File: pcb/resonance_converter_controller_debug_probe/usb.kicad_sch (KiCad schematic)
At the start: 45 parts, among them J1 USB_C_Receptacle_USB2.0_14P, J3 USB_A, J4 USB_C_Receptacle_USB2.0_14P, J5 USB_C_Receptacle_PowerOnly_6P, Q1 Q_PMOS_GDS, Q2 Q_NMOS_GDS, Q3 Q_NMOS_GDS, U17 STUSB4500QTR, U18 USB6B1, U19 FT230XQ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

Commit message: Add schematic for debug probe
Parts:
- J3: footprint (none) -> Connector_USB:USB_A_Molex_67643_Horizontal
- U21, U22: footprint (none) -> Package_SO:TSSOP-8_4.4x3mm_P0.65mm
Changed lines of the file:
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@@
 			)
 		)
-		(property "Footprint" ""
+		(property "Footprint" "Package_SO:TSSOP-8_4.4x3mm_P0.65mm"
 			(at 176.53 121.92 0)
 			(effects
@@
 			)
 		)
-		(property "Footprint" ""
+		(property "Footprint" "Package_SO:TSSOP-8_4.4x3mm_P0.65mm"
 			(at 210.82 175.26 0)
 			(effects
@@
 			)
 		)
-		(property "Footprint" ""
+		(property "Footprint" "Connector_USB:USB_A_Molex_67643_Horizontal"
 			(at 243.84 135.89 0)
 			(effects

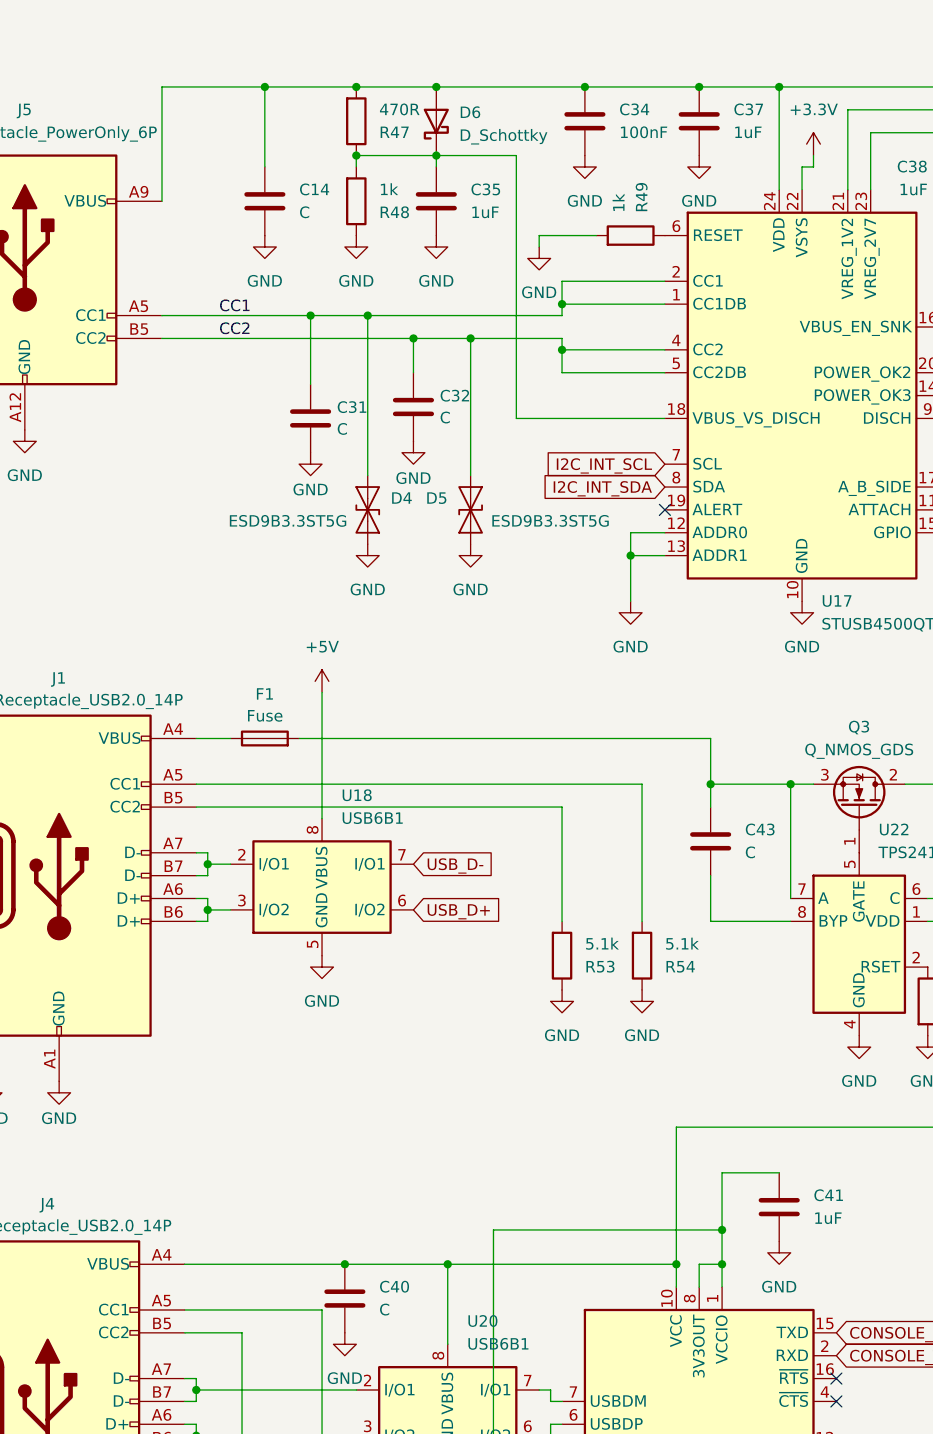
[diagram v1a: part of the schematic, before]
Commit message: Fix schematic and initial component layout
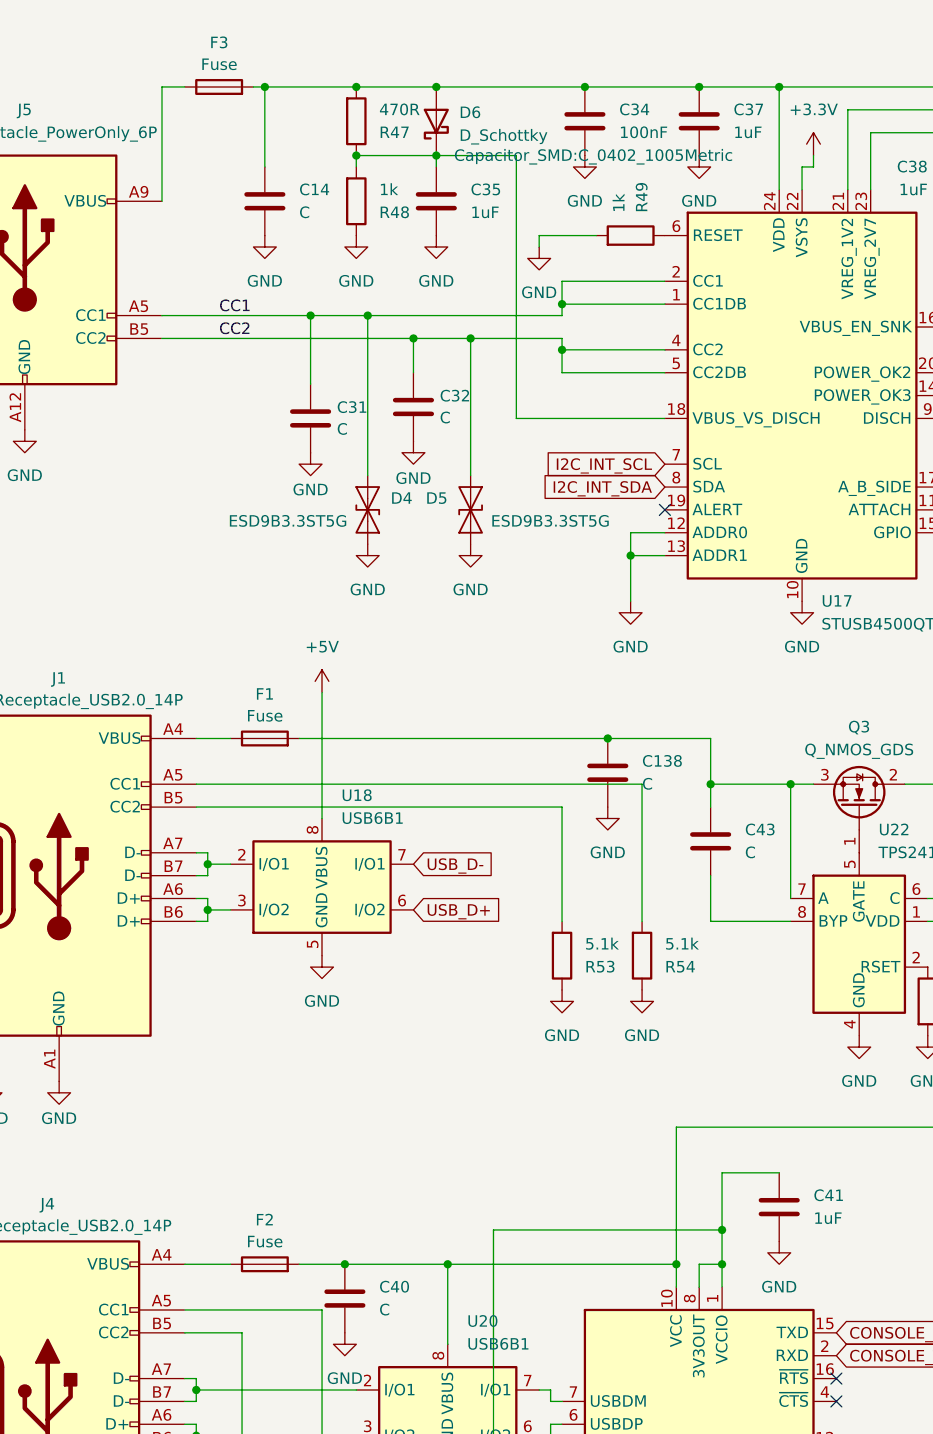
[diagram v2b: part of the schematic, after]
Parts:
- added C138: C, Capacitor_SMD:C_2220_5750Metric, symbol Device:C
- added F2, F3: Fuse, Fuse:Fuse_0805_2012Metric, symbol Device:Fuse
- C34, C36: footprint Capacitor_SMD:C_0805_2012Metric -> Capacitor_SMD:C_0402_1005Metric
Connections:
- net GND: now also C138.2
- net at C40.1, C42.1, Q2.3 (S)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: now also F2.2; no longer J4.A4 (VBUS), J4.A9 (VBUS), J4.B4 (VBUS), J4.B9 (VBUS)
- net at C14.1, C34.1, C37.1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: now also F3.2; no longer J5.A9 (VBUS), J5.B9 (VBUS)
- net at C43.1, F1.2, Q3.3 (S)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: now also C138.1
- new net: F3.1, J5.A9 (VBUS), J5.B9 (VBUS)
- new net: F2.1, J4.A4 (VBUS), J4.A9 (VBUS), J4.B4 (VBUS), J4.B9 (VBUS)
